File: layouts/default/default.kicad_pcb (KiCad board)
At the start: 2 copper layers, 0 parts

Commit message: changed main target to mainboard, added cutoff build, lots of edits to modules
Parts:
- added D1: , lib:SOD-323F_L1.7-W1.3-LS2.5-R-RD, F.Cu at (0.00, -70.0)
- added OLED1: , atopile:OLED-TH_L38.0-W12.0_HS91L02W2C01-1fd193, F.Cu at (0.00, -20.0)
- added U1: 1µF ±10% 25V X5R, atopile:C0402-b3ef17, F.Cu at (0.00, -160.0)
- added U10: 300kΩ ±1% 62.5mW, atopile:R0402-56259e, F.Cu at (0.00, -90.0)
- added U11: 1kΩ ±1% 62.5mW, atopile:R0402-56259e, F.Cu at (0.00, -100.0)
- added U12: 10kΩ ±1% 62.5mW, atopile:R0402-56259e, F.Cu at (0.00, -190.0)
- added U13: 1kΩ ±1% 62.5mW, atopile:R0402-56259e, F.Cu at (0.00, -30.0)
- added U14: 1kΩ ±1% 62.5mW, atopile:R0402-56259e, F.Cu at (0.00, -140.0)
- added U15: 10mΩ ±1% 1W, atopile:R1206-bdb864, F.Cu at (0.00, -40.0)
- added U16: , lib:IND-SMD_L6.6-W6.4, F.Cu at (0.00, -50.0)
- added U17: , lib:CONN-TH_B2B-PH-K-S, F.Cu at (0.00, -80.0)
- added U18: , lib:CONN-TH_B2B-PH-K-S, F.Cu at (0.00, -120.0)
- added U19: , lib:TSSOP-8_L4.4-W3.0-P0.65-LS6.4-BL, F.Cu at (0.00, -150.0)
- added U2: 10µF ±10% 10V X5R, atopile:C0603-bd72f6, F.Cu at (0.00, -170.0)
- added U20: 10µF ±10% 25V X5R, atopile:C0805-3b2e55, F.Cu at (10.0, 0.00)
- added U21: 10µF ±10% 25V X5R, atopile:C0805-3b2e55, F.Cu at (10.0, -30.0)
- added U22: , lib:KEY-SMD_4P-L4.2-W3.2-P2.20-LS4.6, F.Cu at (30.0, 0.00)
- added U23: 10kΩ ±1% 62.5mW, atopile:R0402-56259e, F.Cu at (20.0, 0.00)
- added U24: , lib:WIRELM-SMD_ESP32-S3-WROOM-1, F.Cu at (10.0, -10.0)
- added U25: 100nF ±10% 16V X7R, atopile:C0402-b3ef17, F.Cu at (10.0, -20.0)
- added U26: , atopile:LGA-8_L3.0-W3.0-P0.80-TR-8a5b79, F.Cu at (0.00, 0.00)
- added U27: , atopile:GPSM-SMD_ATGM336H-TR-d79f58, F.Cu at (0.00, -10.0)
- added U3: 100nF ±10% 16V X7R, atopile:C0402-b3ef17, F.Cu at (0.00, -130.0)
- added U4: 4.7µF ±10% 16V X5R, atopile:C0603-bd72f6, F.Cu at (0.00, -20.0)
- added U5: 10µF ±10% 10V X5R, atopile:C0603-bd72f6, F.Cu at (0.00, 0.00)
- added U6: 1nF ±20% 50V X7R, atopile:C0402-b3ef17, F.Cu at (0.00, -110.0)
- added U7: , lib:SOT-23-6_L2.9-W1.6-P0.95-LS2.8-BR, F.Cu at (0.00, -60.0)
- added U8: , lib:SOT-23_L2.9-W1.3-P1.90-LS2.4-BR, F.Cu at (0.00, -180.0)
- added U9: 1MΩ ±1% 62.5mW, atopile:R0402-56259e, F.Cu at (0.00, -10.0)

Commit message: finished cutoff mechanism connections :fixed
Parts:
- added C1: , atopile:CAP-TH_BD8.0-P3.50-D0.6-FD_1-b17e9d, F.Cu at (0.00, -30.0)
- added P1: , atopile:CONN-TH_2P-P9.50_WJ45C-B-2P-7aea0b, F.Cu at (0.00, -10.0)
- added Q1: , atopile:TO-220-3_L10.0-W4.5-P2.54-L-8dee21, F.Cu at (0.00, -20.0)
- added R1: 1kΩ ±1% 62.5mW, atopile:R0402-56259e, F.Cu at (0.00, 0.00)
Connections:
- U14 pad 2: hv-1 -> hv
- U15 pad 2: hv-1 -> hv
- U17 pad 1: hv-1 -> hv
- U20 pad 1: hv -> hv-1
- U21 pad 1: hv -> hv-1
- U23 pad 1: hv -> hv-1
- U24 pad 2: hv -> hv-1
- U25 pad 1: hv -> hv-1
- U5 pad 1: hv-1 -> hv
- U9 pad 1: hv-1 -> hv

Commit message: major updates
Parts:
- removed D1: , lib:SOD-323F_L1.7-W1.3-LS2.5-R-RD
- removed U10: 300kΩ ±1% 62.5mW, atopile:R0402-56259e
- removed U11, U13, U14: 1kΩ ±1% 62.5mW, atopile:R0402-56259e
- removed U12: 10kΩ ±1% 62.5mW, atopile:R0402-56259e
- removed U15: 10mΩ ±1% 1W, atopile:R1206-bdb864
- removed U16: , lib:IND-SMD_L6.6-W6.4
- removed U17, U18: , lib:CONN-TH_B2B-PH-K-S
- removed U19: , lib:TSSOP-8_L4.4-W3.0-P0.65-LS6.4-BL
- removed U5: 10µF ±10% 10V X5R, atopile:C0603-bd72f6
- removed U6: 1nF ±20% 50V X7R, atopile:C0402-b3ef17
- removed U7: , lib:SOT-23-6_L2.9-W1.6-P0.95-LS2.8-BR
- removed U8: , lib:SOT-23_L2.9-W1.3-P1.90-LS2.4-BR
- removed U9: 1MΩ ±1% 62.5mW, atopile:R0402-56259e
- added C10: 100nF ±10% 50V X7R, atopile:C0603-bd72f6, F.Cu at (0.00, 0.00)
- added C11: 100nF ±10% 50V X7R, atopile:C0603-bd72f6, F.Cu at (0.00, -10.0)
- added C2: 100nF ±10% 16V X7R, atopile:C0402-b3ef17, F.Cu at (10.0, -140.0)
- added C3: 100nF ±10% 16V X7R, atopile:C0402-b3ef17, F.Cu at (10.0, -150.0)
- added C4: 100nF ±10% 16V X7R, atopile:C0402-b3ef17, F.Cu at (10.0, -170.0)
- added C5: 100nF ±10% 16V X7R, atopile:C0402-b3ef17, F.Cu at (10.0, 0.00)
- added C6: 100nF ±10% 16V X7R, atopile:C0402-b3ef17, F.Cu at (10.0, -10.0)
- added C7: 100nF ±10% 16V X7R, atopile:C0402-b3ef17, F.Cu at (10.0, -70.0)
- added C8: 100nF ±10% 16V X7R, atopile:C0402-b3ef17, F.Cu at (10.0, -20.0)
- added C9: 100nF ±10% 16V X7R, atopile:C0402-b3ef17, F.Cu at (10.0, -110.0)
- added D2: , atopile:SMA_L4.3-W2.6-LS5.2-RD-e14692, F.Cu at (10.0, -20.0)
- added LED1: , atopile:SENSOR-TH_BPW34-c0a4b0, F.Cu at (10.0, -200.0)
- added LED2: , atopile:SENSOR-TH_BPW34-c0a4b0, F.Cu at (10.0, -120.0)
- added LED3: , atopile:SENSOR-TH_BPW34-c0a4b0, F.Cu at (10.0, -130.0)
- added LED4: , atopile:SENSOR-TH_BPW34-c0a4b0, F.Cu at (10.0, -210.0)
- added Q2: , atopile:TO-220-3_L10.0-W4.5-P2.54-L-8dee21, F.Cu at (10.0, 0.00)
- added R10: 1kΩ ±1% 50mW, atopile:R0201-27027e, F.Cu at (10.0, -60.0)
- added R11: 1kΩ ±1% 50mW, atopile:R0201-27027e, F.Cu at (10.0, -90.0)
- added R12: 10kΩ ±1% 100mW, atopile:R0603-ebcab9, F.Cu at (10.0, -100.0)
- added R13: 1kΩ ±1% 50mW, atopile:R0201-27027e, F.Cu at (10.0, -30.0)
- added R2: 10kΩ ±1% 62.5mW, atopile:R0402-56259e, F.Cu at (0.00, -20.0)
- added R3: 10kΩ ±1% 62.5mW, atopile:R0402-56259e, F.Cu at (0.00, -10.0)
- added R4: 10kΩ ±1% 62.5mW, atopile:R0402-56259e, F.Cu at (0.00, 0.00)
- added R5: 1kΩ ±1% 50mW, atopile:R0201-27027e, F.Cu at (10.0, -180.0)
- added R6: 1kΩ ±1% 50mW, atopile:R0201-27027e, F.Cu at (10.0, -40.0)
- added R7: 1kΩ ±1% 50mW, atopile:R0201-27027e, F.Cu at (10.0, -160.0)
- added R8: 1kΩ ±1% 50mW, atopile:R0201-27027e, F.Cu at (10.0, -80.0)
- added R9: 1kΩ ±1% 50mW, atopile:R0201-27027e, F.Cu at (10.0, -190.0)
- added U28: , atopile:WIRELM-SMD_E22-900M30S-98c301, F.Cu at (0.00, -10.0)
- R1: value 1kΩ ±1% 62.5mW -> 10kΩ ±1% 62.5mW
- U1: value 1µF ±10% 25V X5R -> (none); footprint atopile:C0402-b3ef17 -> atopile:SOIC-8_L5.0-W4.0-P1.27-LS6.0-BL-294f77
- U2: value 10µF ±10% 10V X5R -> (none); footprint atopile:C0603-bd72f6 -> lib:SOT-223-3_L6.5-W3.4-P2.30-LS7.0-BR
- U26: footprint atopile:LGA-8_L3.0-W3.0-P0.80-TR-8a5b79 -> atopile:LGA-8_L3.0-W3.0-P0.80_BME688-7465bb
- U3: value 100nF ±10% 16V X7R -> 10µF ±10% 25V X5R; footprint atopile:C0402-b3ef17 -> atopile:C0805-3b2e55
- U4: value 4.7µF ±10% 16V X5R -> 10µF ±10% 25V X5R; footprint atopile:C0603-bd72f6 -> atopile:C0805-3b2e55
- moved U2 170.0 mm to (0.00, 0.00)
- moved U3 120.0 mm to (0.00, -10.0)
- moved U1 110.5 mm to (10.0, -50.0)
- moved Q1 14.1 mm to (10.0, -10.0)
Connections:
- net unnamed[1] renamed cutoff-K
- C1 pad 2: cutoff-gnd -> cutoff-C
- OLED1 pad 1: oled-gnd -> gnd
- OLED1 pad 2: oled-VCC -> hv
- OLED1 pad 3: oled-SCL -> SCL
- OLED1 pad 4: oled-SDA -> SDA
- P1 pad 2: C -> cutoff-C-1
- Q1 pad 1: GATE -> SC_GATE
- Q1 pad 2: C -> cutoff-C
- Q1 pad 3: cutoff-gnd -> gnd-1
- R1 pad 1: cutoff-hv -> hv-2
- U1 pad 1: ICTRL_PLUS -> OUT1
- U1 pad 2: ICTRL_MINUS -> detector-K
- U2 pad 1: S -> gnd
- U2 pad 2: gnd -> hv
- U20 pad 1: hv-1 -> hv
- U20 pad 2: gnd-1 -> gnd
- U21 pad 1: hv-1 -> hv
- U21 pad 2: gnd-1 -> gnd
- U22 pad 3: gnd-1 -> gnd
- U22 pad 4: gnd-1 -> gnd
- U23 pad 1: hv-1 -> hv
- U24 pad 1: gnd-1 -> gnd
- U24 pad 2: hv-1 -> hv
- U24 pad 27: io0 -> SC_GATE
- U24 pad 38: io2 -> out
- U24 pad 39: io1 -> CUTOFF_GATE
- U24 pad 40: gnd-1 -> gnd
- U24 pad 41: gnd-1 -> gnd
- U24 pad 6: io6 -> SCL
- U24 pad 7: io7 -> SDA
- U25 pad 1: hv-1 -> hv
- U25 pad 2: gnd-1 -> gnd
- U26 pad 1: GND -> gnd
- U26 pad 3: SDI -> SDA
- U26 pad 4: SCK -> SCL
- U26 pad 5: SDO -> gnd
- U26 pad 6: VDDIO -> CSB
- U26 pad 7: GND -> gnd
- U26 pad 8: VDD -> hv
- U27 pad 1: gps-gnd -> gnd
- U27 pad 10: gps-gnd -> gnd
- U27 pad 12: gps-gnd -> gnd
- U27 pad 14: VCC_RF -> hv
- U27 pad 16: gps-SDA -> SDA
- U27 pad 17: gps-SCL -> SCL
- U27 pad 8: gps-VCC -> hv
- U3 pad 1: XSHUT -> hv-1
- U4 pad 1: VOUT -> hv

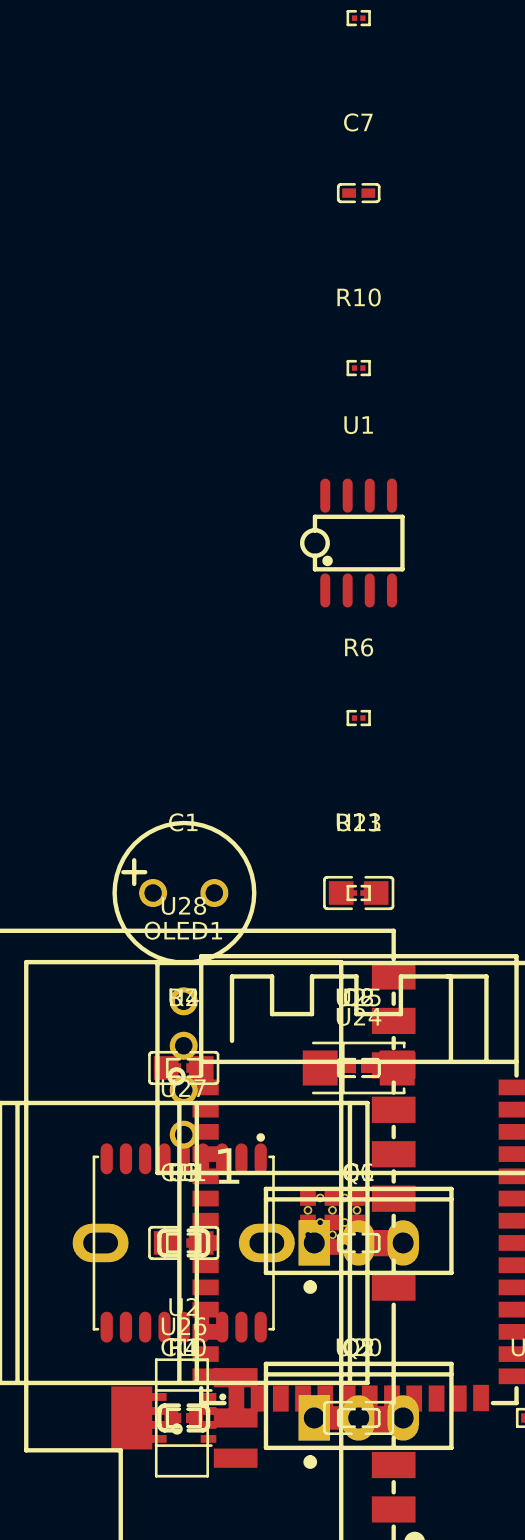
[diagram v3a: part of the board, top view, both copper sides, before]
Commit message: added boost buck
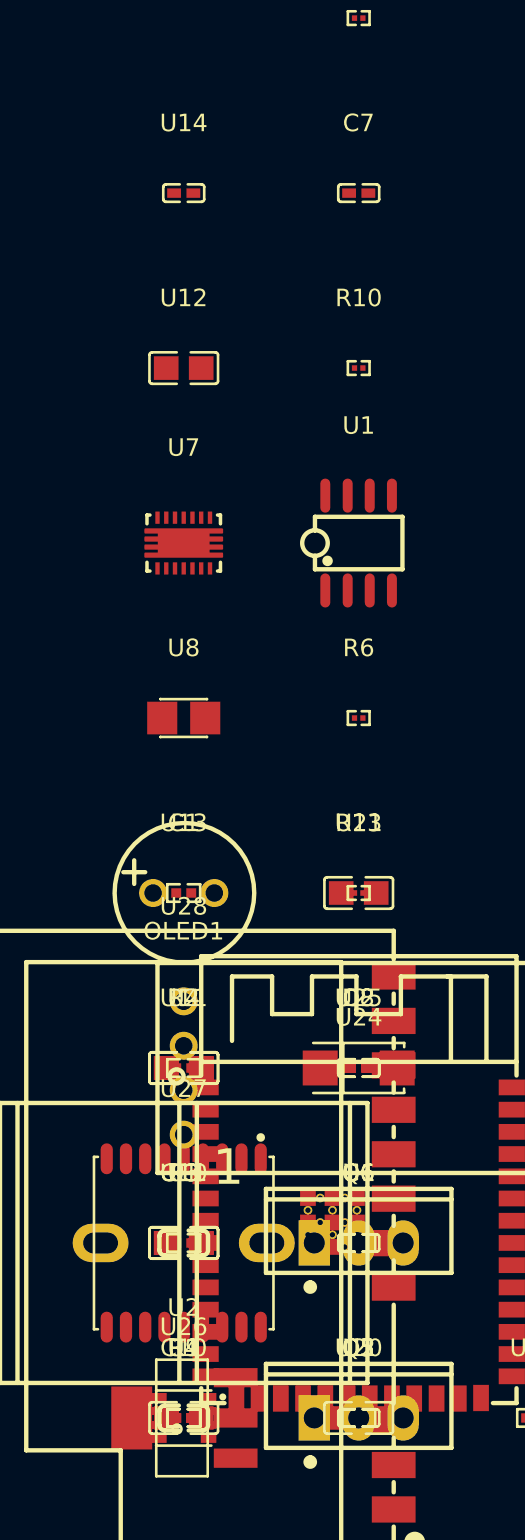
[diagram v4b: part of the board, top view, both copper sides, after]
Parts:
- added U10: 10µF ±10% 25V X5R, atopile:C0805-3b2e55, F.Cu at (0.00, -10.0)
- added U11: 10µF ±10% 25V X5R, atopile:C0805-3b2e55, F.Cu at (0.00, -20.0)
- added U12: 10µF ±10% 25V X5R, atopile:C0805-3b2e55, F.Cu at (0.00, -60.0)
- added U13: 1MΩ ±1% 62.5mW, atopile:R0402-56259e, F.Cu at (0.00, -30.0)
- added U14: 100nF ±10% 16V X7R, atopile:C0402-b3ef17, F.Cu at (0.00, -70.0)
- added U5: 180kΩ ±1% 62.5mW, atopile:R0402-56259e, F.Cu at (10.0, 0.00)
- added U6: 1.6MΩ ±1% 62.5mW, atopile:R0402-56259e, F.Cu at (10.0, -10.0)
- added U7: , lib:VSON-14_L4.0-W3.0-P0.50-BL-EP_TI_DSJ, F.Cu at (0.00, -50.0)
- added U8: 1.5µH ±20%, lib:IND-SMD_L2.5-W2.0_WPN252012H, F.Cu at (0.00, -40.0)
- added U9: 10µF ±10% 25V X5R, atopile:C0805-3b2e55, F.Cu at (0.00, 0.00)
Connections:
- net CSB renamed VDDIO
- net detector-net-1 renamed unnamed[1]
- C1 pad 2: cutoff-C -> cutoff-C-1
- C10 pad 2: gnd-1 -> gnd
- C11 pad 2: gnd-1 -> gnd
- C5 pad 2: gnd-1 -> gnd
- C7 pad 2: gnd-1 -> gnd
- C8 pad 2: gnd-1 -> gnd
- D2 pad 2: gnd-1 -> gnd
- LED1 pad 1: gnd-1 -> gnd
- LED2 pad 1: gnd-1 -> gnd
- LED3 pad 1: gnd-1 -> gnd
- LED4 pad 1: gnd-1 -> gnd
- P1 pad 2: cutoff-C-1 -> cutoff-C
- Q1 pad 2: cutoff-C -> cutoff-C-1
- Q1 pad 3: gnd-1 -> gnd
- Q2 pad 2: cutoff-C-1 -> cutoff-C
- Q2 pad 3: gnd-1 -> gnd
- R11 pad 2: gnd-1 -> gnd
- R13 pad 2: gnd-1 -> gnd
- R2 pad 2: gnd-1 -> gnd
- R3 pad 2: gnd-1 -> gnd
- R6 pad 2: gnd-1 -> gnd
- U1 pad 4: gnd-1 -> gnd
- U28 pad 1: gnd-1 -> gnd
- U28 pad 11: gnd-1 -> gnd
- U28 pad 12: gnd-1 -> gnd
- U28 pad 2: gnd-1 -> gnd
- U28 pad 20: gnd-1 -> gnd
- U28 pad 22: gnd-1 -> gnd
- U28 pad 3: gnd-1 -> gnd
- U28 pad 4: gnd-1 -> gnd
- U28 pad 5: gnd-1 -> gnd

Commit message: pcb layout
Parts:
- added U15: , lib:WSON-10_L2.0-W2.0-P0.40-BL-EP, F.Cu at (75.0, 69.5)
- added U16: 1µF ±10% 25V X5R, atopile:C0402-b3ef17, F.Cu at (73.3, 70.2)
- added U17: 549Ω ±0% 62.5mW, atopile:R0402-56259e, F.Cu at (76.7, 68.3)
- added U18: 1µF ±10% 25V X5R, atopile:C0402-b3ef17, F.Cu at (76.7, 70.2)
- added U19: 4.7kΩ ±1% 62.5mW, atopile:R0402-56259e, F.Cu at (41.1, 50.8)
- added U29: 4.7kΩ ±1% 62.5mW, atopile:R0402-56259e, F.Cu at (41.1, 53.8)
- added U30: , lib:USB-C-SMD_KH-TYPE-C-16P, F.Cu at (36.6, 52.0)
- U6: value 1.6MΩ ±1% 62.5mW -> 1.6MΩ ±5% 62.5mW
- moved LED4 245.1 mm to (85.2, 23.2), turned to 90 degrees
- moved LED1 240.2 mm to (98.7, 23.2), turned to 90 degrees
- moved R9 221.0 mm to (78.1, 20.2), turned to 180 degrees
- moved C2 181.8 mm to (76.4, 29.2), turned to 180 degrees
- moved LED3 172.7 mm to (89.7, 23.2), turned to 90 degrees
- moved LED2 166.1 mm to (94.2, 23.2), turned to 90 degrees
- moved C9 151.6 mm to (74.0, 27.5)
- moved C3 147.6 mm to (78.1, -19.0)
- moved C4 147.6 mm to (78.1, -39.0)
- moved R5 147.6 mm to (78.1, -49.0)
- moved R7 147.6 mm to (78.1, -29.0)
- moved U14 143.6 mm to (58.0, 61.4), turned to -90 degrees
- moved U12 134.1 mm to (62.5, 58.6), turned to -90 degrees
- moved U28 123.6 mm to (97.7, 65.8), turned to 90 degrees
- moved U7 121.9 mm to (56.5, 58.0), turned to 90 degrees
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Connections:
- net PG renamed boostbuck-PG
- net VINA renamed EN
- net dm renamed uc-dm
- net dp renamed uc-dp
- C10 pad 1: hv-2 -> hv
- C11 pad 1: hv-2 -> hv
- C4 pad 2: detector-net -> detector-net-1
- C5 pad 1: hv-2 -> hv
- C8 pad 1: unnamed[1] -> detector-net
- C9 pad 1: unnamed[1] -> detector-net
- OLED1 pad 2: hv -> hv-3
- R1 pad 1: hv-2 -> hv
- R10 pad 1: hv-2 -> hv
- R12 pad 2: unnamed[1] -> detector-net
- R5 pad 1: hv-2 -> hv
- R8 pad 1: detector-net -> detector-net-1
- U1 pad 8: hv-2 -> hv
- U11 pad 1: hv-2 -> hv
- U12 pad 1: hv-2 -> hv
- U2 pad 2: hv -> hv-3
- U2 pad 4: hv -> hv-3
- U20 pad 1: hv -> hv-3
- U21 pad 1: hv -> hv-3
- U23 pad 1: hv -> hv-3
- U24 pad 2: hv -> hv-3
- U25 pad 1: hv -> hv-3
- U26 pad 8: hv -> hv-3
- U27 pad 14: hv -> hv-3
- U27 pad 8: hv -> hv-3
- U28 pad 10: hv-2 -> hv
- U28 pad 9: hv-2 -> hv
- U4 pad 1: hv -> hv-3
- U6 pad 1: hv-2 -> hv
- U7 pad 4: hv-2 -> hv
- U7 pad 5: hv-2 -> hv
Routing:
- net gnd: track 0.00 -> 12.0 mm
- net in: track 0.00 -> 8.40 mm
- net hv-3: track 0.00 -> 7.15 mm
- net hv-1: track 0.00 -> 6.80 mm
- net hv-2: track 0.00 -> 6.47 mm, vias 0 -> 2
- net hv: track 0.00 -> 6.20 mm
- net ISET: track 0.00 -> 2.76 mm
- net L1: track 0.00 -> 2.59 mm
- net L2: track 0.00 -> 2.54 mm
- net FB: track 0.00 -> 2.08 mm
- net CC2: track 0.00 -> 1.65 mm
- net A5: track 0.00 -> 1.60 mm
- net EN: track 0.00 -> 1.41 mm
- net boostbuck-PG: track 0.00 -> 1.29 mm
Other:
- board outline added: 88 x 62 mm

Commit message: save
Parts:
- U6: value 1.6MΩ ±5% 62.5mW -> 1.6MΩ ±1% 62.5mW
- moved R13 95.7 mm to (70.5, 25.0), turned to 90 degrees
- moved C8 91.3 mm to (72.0, 24.5), turned to 90 degrees
- moved C5 85.5 mm to (75.5, 21.0), turned to 180 degrees
- moved R12 75.6 mm to (74.0, 25.8), turned to -90 degrees
- moved R7 60.6 mm to (77.0, 31.5), turned to 180 degrees
- moved R8 51.5 mm to (75.8, 19.5)
- moved C9 2.65 mm to (71.5, 26.5), turned to 180 degrees
- moved R10 1.44 mm to (75.0, 23.2), turned to -90 degrees
- moved C2 1.12 mm to (76.9, 30.2)
- moved C6 1.12 mm to (78.5, 20.0)
- moved R6 1.12 mm to (79.5, 30.0)
- moved R9 1.12 mm to (78.6, 21.2)
- moved U1 1.12 mm to (78.4, 25.7)
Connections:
- net CC2 renamed B5
- net EN renamed VINA
- net FB renamed boostbuck-out
- net SUB1 renamed A8
- C1 pad 2: cutoff-C-1 -> cutoff-C
- C10 pad 1: hv -> hv-2
- C11 pad 1: hv -> hv-2
- C5 pad 1: hv -> hv-2
- P1 pad 2: cutoff-C -> cutoff-C-1
- Q1 pad 2: cutoff-C-1 -> cutoff-C
- Q2 pad 2: cutoff-C -> cutoff-C-1
- R1 pad 1: hv -> hv-2
- R10 pad 1: hv -> hv-2
- R5 pad 1: hv -> hv-2
- U1 pad 8: hv -> hv-2
- U11 pad 1: hv -> hv-2
- U12 pad 1: hv -> hv-2
- U15 pad 1: hv-2 -> hv
- U15 pad 7: hv-2 -> hv
- U16 pad 1: hv-2 -> hv
- U28 pad 10: hv -> hv-2
- U28 pad 9: hv -> hv-2
- U30 pad A4: hv-2 -> hv
- U30 pad A9: hv-2 -> hv
- U30 pad B4: hv-2 -> hv
- U30 pad B9: hv-2 -> hv
- U6 pad 1: hv -> hv-2
- U7 pad 4: hv -> hv-2
- U7 pad 5: hv -> hv-2
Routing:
- net hv-2: track 6.47 -> 6.20 mm, vias 2 -> 0
- net hv: track 6.20 -> 6.47 mm, vias 0 -> 2

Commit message: built
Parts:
- removed U28: , atopile:WIRELM-SMD_E22-900M30S-98c301
- removed U3, U4: 10µF ±10% 25V X5R, atopile:C0805-3b2e55
- added R14: 1kΩ ±1% 62.5mW, atopile:R0402-56259e, F.Cu at (0.00, 0.00)
- added R15: 1kΩ ±1% 62.5mW, atopile:R0402-56259e, F.Cu at (0.00, -10.0)
- C10: footprint atopile:C0603-bd72f6 -> atopile:C0805-3b2e55
- C11: value 100nF ±10% 50V X7R -> 100nF ±10% 16V X7R; footprint atopile:C0603-bd72f6 -> atopile:C0402-b3ef17
- R1, R2, R3, R4: value 10kΩ ±1% 62.5mW -> 1kΩ ±1% 62.5mW
- R10, R11, R13, R5, R6, R7, R8, R9: value 1kΩ ±1% 50mW -> 0Ω 50mW
- U17: value 549Ω ±0% 62.5mW -> 560Ω ±1% 62.5mW
- U2: footprint lib:SOT-223-3_L6.5-W3.4-P2.30-LS7.0-BR -> atopile:WIRELM-SMD_E22-900M30S-98c301
- U5: value 180kΩ ±1% 62.5mW -> 820Ω ±1% 62.5mW
- U6: value 1.6MΩ ±1% 62.5mW -> 4.7kΩ ±1% 62.5mW
- moved U2 104.1 mm to (0.00, -40.0), turned to 0 degrees
- moved C10 37.6 mm to (0.00, -20.0)
- moved C11 20.0 mm to (0.00, -30.0)
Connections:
- net A5 renamed CC1
- net A8 renamed SUB1
- net VDDIO renamed CSB
- net boostbuck-out renamed FB
- net tck renamed io39
- net tdi renamed io41
- net tdo renamed io40
- net tms renamed io42
- net uc-dm renamed io19
- net uc-dp renamed io20
- net usbc-dm renamed DN1
- net usbc-dp renamed DP1
- C1 pad 2: cutoff-C -> cutoff-C-1
- C10 pad 1: hv-2 -> hv
- C11 pad 1: hv-2 -> hv
- C3 pad 1: detector.C3-net-1 -> hv
- C3 pad 2: detector.C3-net -> gnd
- C5 pad 1: hv-2 -> hv
- OLED1 pad 2: hv-3 -> hv-1
- P1 pad 2: cutoff-C-1 -> cutoff-C
- Q1 pad 2: cutoff-C -> cutoff-C-1
- Q2 pad 2: cutoff-C-1 -> cutoff-C
- R1 pad 1: hv-2 -> hv
- R10 pad 1: hv-2 -> hv
- R5 pad 1: hv-2 -> hv
- U1 pad 8: hv-2 -> hv
- U10 pad 1: hv-1 -> hv-3
- U11 pad 1: hv-2 -> hv
- U12 pad 1: hv-2 -> hv
- U15 pad 1: hv -> hv-2
- U15 pad 10: hv-1 -> hv-3
- U15 pad 7: hv -> hv-2
- U16 pad 1: hv -> hv-2
- U18 pad 1: hv-1 -> hv-3
- U2 pad 2: hv-3 -> gnd
- U2 pad 3: hv-1 -> gnd
- U2 pad 4: hv-3 -> gnd
- U20 pad 1: hv-3 -> hv-1
- U21 pad 1: hv-3 -> hv-1
- U23 pad 1: hv-3 -> hv-1
- U24 pad 18: cs -> io10
- U24 pad 19: mosi -> io11
- U24 pad 2: hv-3 -> hv-1
- U24 pad 20: sck -> io12
- U24 pad 21: miso -> io13
- U24 pad 3: in -> EN
- U25 pad 1: hv-3 -> hv-1
- U26 pad 8: hv-3 -> hv-1
- U27 pad 14: hv-3 -> hv-1
- U27 pad 8: hv-3 -> hv-1
- U30 pad A4: hv -> hv-2
- U30 pad A9: hv -> hv-2
- U30 pad B4: hv -> hv-2
- U30 pad B9: hv -> hv-2
- U6 pad 1: hv-2 -> hv
- U7 pad 10: hv-1 -> hv-3
- U7 pad 11: hv-1 -> hv-3
- U7 pad 4: hv-2 -> hv
- U7 pad 5: hv-2 -> hv
- U9 pad 1: hv-1 -> hv-3
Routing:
- net hv: track 6.47 -> 0.00 mm, vias 2 -> 0
- net (no net): track 0.00 -> 6.20 mm
- net hv-2: track 6.20 -> 6.47 mm, vias 0 -> 2

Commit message: layout updates
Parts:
- removed OLED1: , atopile:OLED-TH_L38.0-W12.0_HS91L02W2C01-1fd193
- removed U26: , atopile:LGA-8_L3.0-W3.0-P0.80_BME688-7465bb
- P1: footprint atopile:CONN-TH_2P-P9.50_WJ45C-B-2P-7aea0b -> atopile:CONN-TH_2P-P5.00_WJ128V-5.0-2P-75f14f
- moved U2 138.0 mm to (88.8, 65.6), turned to 90 degrees
- moved C11 110.6 mm to (75.2, 51.1), turned to 180 degrees
- moved R15 102.3 mm to (82.0, 51.2)
- moved C10 101.7 mm to (69.6, 54.1), turned to 90 degrees
- moved R2 99.6 mm to (49.0, 68.2)
- moved R14 98.7 mm to (84.4, 51.2)
- moved R3 96.6 mm to (57.1, 69.4), turned to 180 degrees
- moved R5 94.4 mm to (78.2, 45.3)
- moved C4 84.9 mm to (82.2, 45.7), turned to -90 degrees
- moved R4 83.9 mm to (48.5, 70.0), turned to 90 degrees
- moved R1 83.1 mm to (47.1, 70.0), turned to -90 degrees
- moved R11 79.5 mm to (77.6, 38.7), turned to 90 degrees
- moved C3 65.5 mm to (78.6, 46.5)
- moved C7 59.8 mm to (76.4, 38.3), turned to 90 degrees
- moved U30 34.1 mm to (67.8, 38.3), turned to 180 degrees
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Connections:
- net B5 renamed CC2
- net CC1 renamed A5
- net DN1 renamed DN2
- net DP1 renamed DP2
- C10 pad 1: hv -> hv-2
- C11 pad 1: hv -> hv-2
- C3 pad 1: hv -> hv-2
- C4 pad 2: detector-net-1 -> detector-net
- C5 pad 1: hv -> hv-2
- C8 pad 1: detector-net -> detector-net-1
- C9 pad 1: detector-net -> detector-net-1
- R1 pad 1: hv -> hv-2
- R10 pad 1: hv -> hv-2
- R12 pad 2: detector-net -> detector-net-1
- R14 pad 1: hv -> hv-2
- R15 pad 1: hv -> hv-2
- R5 pad 1: hv -> hv-2
- R8 pad 1: detector-net-1 -> detector-net
- U1 pad 8: hv -> hv-2
- U10 pad 1: hv-3 -> hv
- U11 pad 1: hv -> hv-2
- U12 pad 1: hv -> hv-2
- U15 pad 1: hv-2 -> hv-1
- U15 pad 10: hv-3 -> hv
- U15 pad 7: hv-2 -> hv-1
- U16 pad 1: hv-2 -> hv-1
- U18 pad 1: hv-3 -> hv
- U2 pad 10: hv -> hv-2
- U2 pad 9: hv -> hv-2
- U20 pad 1: hv-1 -> hv-3
- U21 pad 1: hv-1 -> hv-3
- U23 pad 1: hv-1 -> hv-3
- U24 pad 2: hv-1 -> hv-3
- U24 pad 3: EN -> in
- U25 pad 1: hv-1 -> hv-3
- U27 pad 14: hv-1 -> hv-3
- U27 pad 8: hv-1 -> hv-3
- U30 pad A4: hv-2 -> hv-1
- U30 pad A9: hv-2 -> hv-1
- U30 pad B4: hv-2 -> hv-1
- U30 pad B9: hv-2 -> hv-1
- U6 pad 1: hv -> hv-2
- U7 pad 10: hv-3 -> hv
- U7 pad 11: hv-3 -> hv
- U7 pad 4: hv -> hv-2
- U7 pad 5: hv -> hv-2
- U9 pad 1: hv-3 -> hv
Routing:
- net gnd: track 12.0 -> 110.4 mm, vias 0 -> 3
- net hv-2: track 6.47 -> 36.4 mm, vias 2 -> 0
- net detector-K: track 0.00 -> 19.1 mm
- net OUT2: track 0.00 -> 17.4 mm, vias 0 -> 2
- net IN2minus: track 0.00 -> 11.3 mm, vias 0 -> 2
- net IN2plus: track 0.00 -> 10.4 mm
- net IN1plus: track 0.00 -> 7.96 mm
- net hv: track 0.00 -> 6.80 mm
- net (no net): track 6.20 -> 0.00 mm
- net OUT1: track 0.00 -> 5.03 mm
- net RXEN: track 0.00 -> 4.05 mm
- net TXEN: track 0.00 -> 3.23 mm
- net detector-net-1: track 0.00 -> 2.82 mm
- net out: track 0.00 -> 1.42 mm
- net detector-net: track 0.00 -> 1.23 mm
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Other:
- board size 88 x 62 mm -> 76.8 x 46.3 mm
